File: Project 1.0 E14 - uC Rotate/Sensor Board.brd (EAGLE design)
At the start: 38.5 x 75 mm, 106 parts, among them IC1 LT1963EST-1.5, IC2 LT1963EST-1.5, IC4 LT1963EST-1.5, J1 501568-0207, J2 501568-0207, J3 SD-105027-101, J4 501568-0407, U1 MAG3110, U10 ADXL362, U11 TM4C1233H6PM, U14 TXB0108, U15 ADT7301, U17 LSM9DS0, U19 MAX21000, U2 H3LIS331DLTR, U21 SN74HC42, U22 SI7013, U3 L3GD20H, U4 LPS331AP, U5 MPL3115A2, U6 LSM303D, U8 STLM20, U9 LIS3DH, X1 32.768 kHz, X2 16.000 MHz

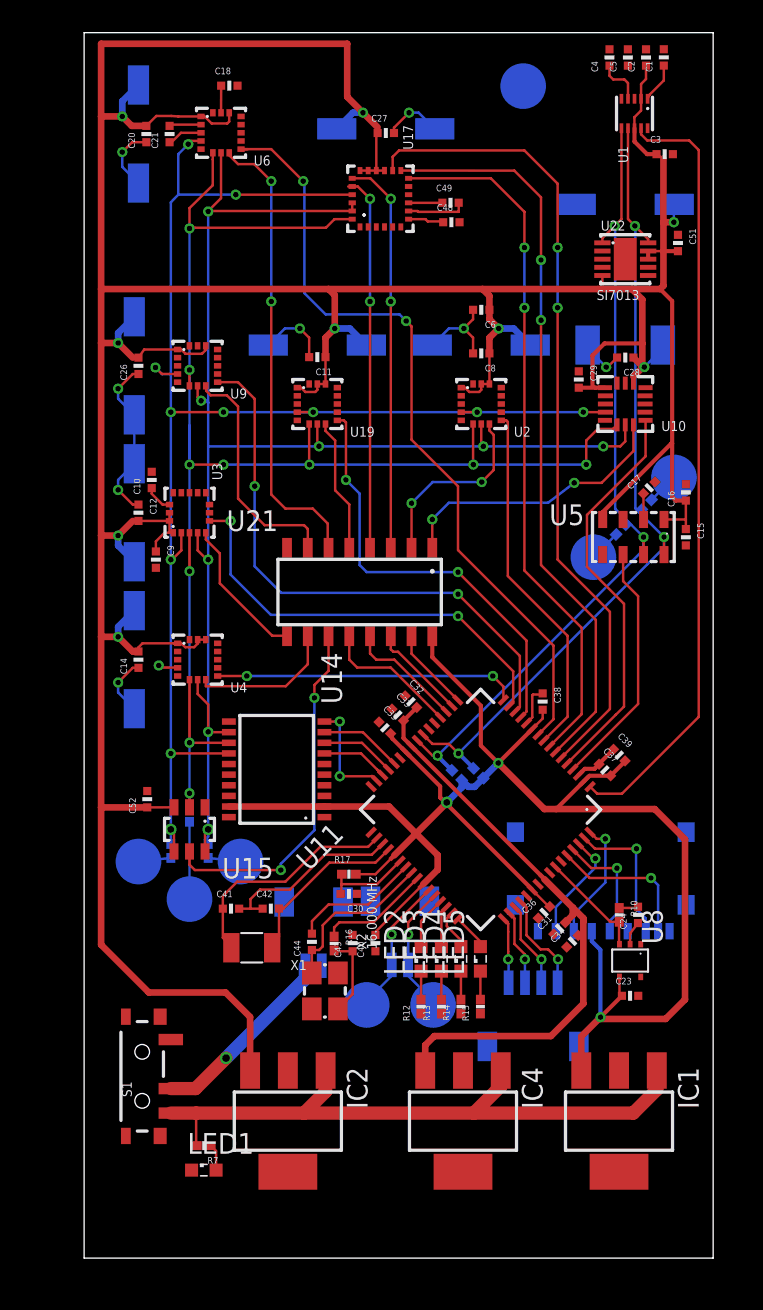
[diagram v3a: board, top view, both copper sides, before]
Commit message: Sensor Test Board: Completed power routing, Removed 1.2V regulator as this is not needed per the Tiva c datasheet. Power regulators and their respective circuits have been added for both 3.3-A and 3.3-B power rails. Swich has been moved to the bottom layer and is now positined facing the bottom of the board.
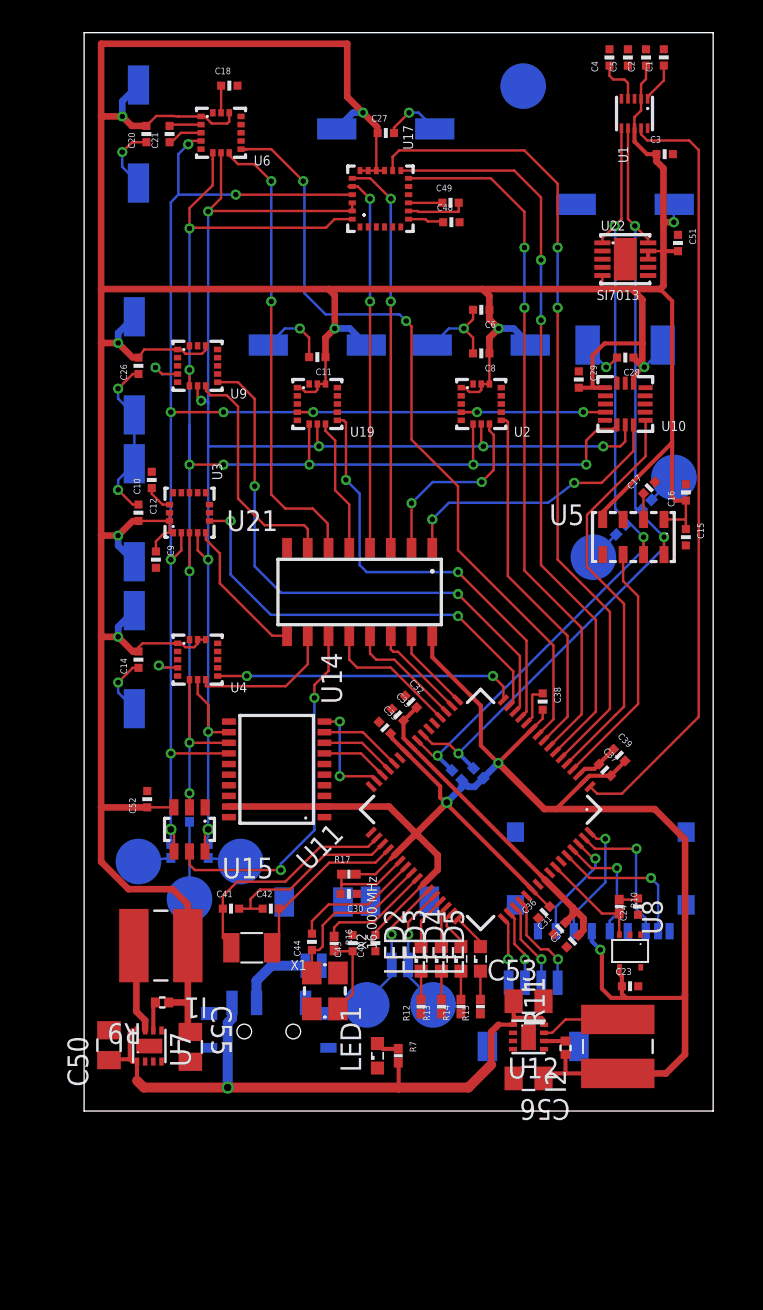
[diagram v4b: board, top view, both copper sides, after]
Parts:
- removed IC1, IC2, IC4: LT1963EST-1.5, linear-technology:SOT223
- added C50, C53: GRM21BR60J106ME19L, Power Regulator:0805
- added C55, C56: C2012X5R0J226M, Power Regulator:0805
- added I1, I2: SDR0403-1R0ML, Power Regulator:SDR0403
- added R11, R9: CRCW0402178KFKED, Power Regulator:0402
- added U12, U7: TPS62082DSGR, Power Regulator:S-PWSON-N8
- moved R7 13.1 mm to (20.7, 12.4), turned to 270 degrees
- moved LED1 12.7 mm to (19.5, 12.4), turned to 90 degrees
- moved S1 8.22 mm to (12.8, 13.9), flipped to the bottom, turned to 180 degrees
- moved C23 0.58 mm to (34.9, 16.6)
- moved U8 0.58 mm to (34.9, 18.8)
- moved C24 0.51 mm to (35.4, 21.5)
- moved R10 0.51 mm to (34.3, 21.5)
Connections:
- new net N$13: I1.2, U7.7
- new net N$23: R9.2, U7.6
- new net N$36: I2.2, U12.7
- new net N$37: R11.2, U12.6
- net 1.2V: no longer IC4.3
- net 3.3V-A: now also C55.1, I1.1, R9.1; no longer IC2.3
- net 3.3V-B: now also C56.1, I2.1, R11.1; no longer IC1.3
- net GND: now also C50.2, C53.2, C55.2, C56.2, U12.2, U12.3, U12.9, U7.2, U7.3, U7.9; no longer IC1.2, IC1.4, IC2.2, IC2.4, IC4.2, IC4.4
- net POWER-IN: now also C50.1, C53.1, U12.1, U12.8, U7.1, U7.8; no longer IC1.1, IC2.1, IC4.1
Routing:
- net 1.2V: track 37.5 -> 20.2 mm
- net N$2: track 11.8 -> 4.73 mm, vias 1 -> 0
- net 3.3V-B: track 110.9 -> 117.7 mm
- net N$13: track 0.00 -> 5.48 mm
- net N$36: track 0.00 -> 4.85 mm
- net 3.3V-A: track 257.4 -> 253.4 mm
- net POWER-IN: track 40.0 -> 41.9 mm, vias 0 -> 1
- net N$23: track 0.00 -> 1.77 mm
- net GND: track 60.6 -> 59.2 mm
- net N$37: track 0.00 -> 1.31 mm
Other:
- board size 38.5 x 75 mm -> 38.5 x 66 mm

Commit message: Sensor Test Board: Corrected LED footprint, Rerouted power under the uC to remove power traces from directly under uC. Moved sensor power rail further from edge of PCB to allow for GND plain to fully surround power rail.
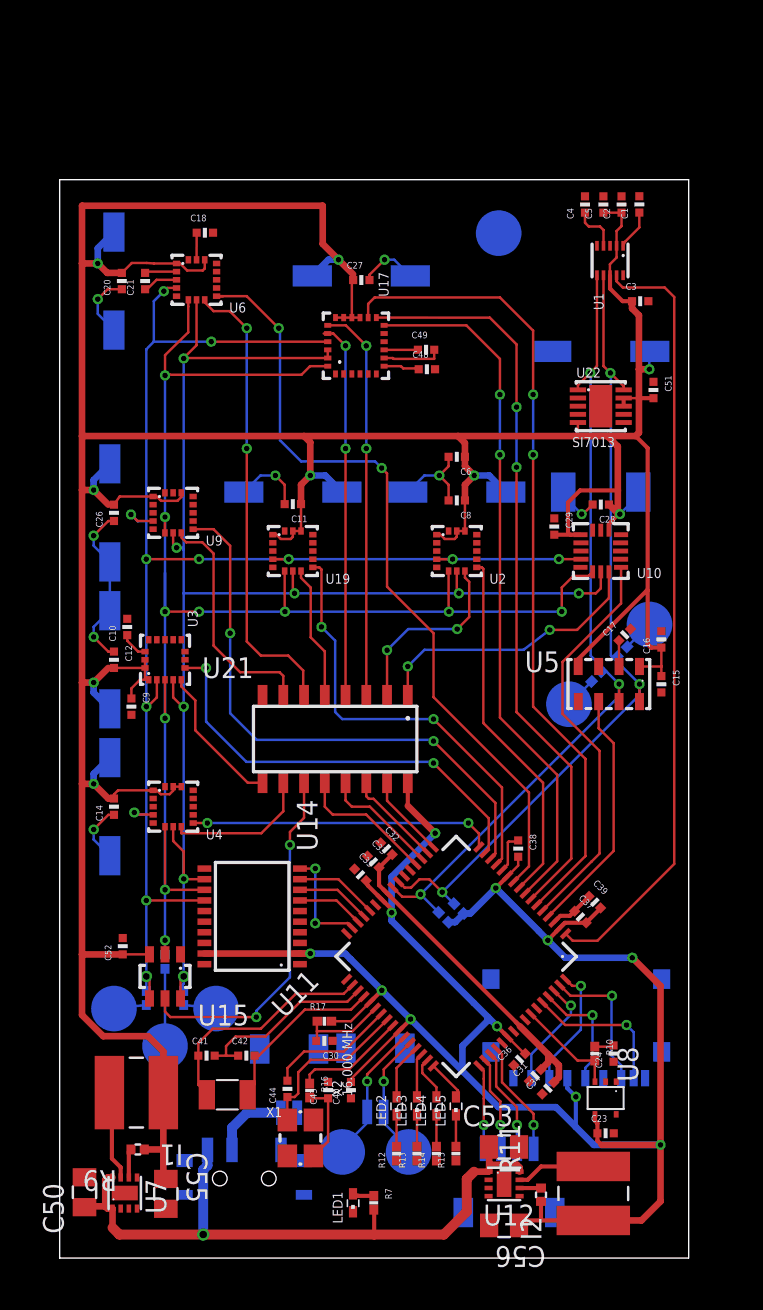
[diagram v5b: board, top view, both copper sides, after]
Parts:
- LED1: device eagle-ltspice:LED_SML0603 -> Kas-Diodes-LEDs:LED_0402
- LED2, LED3, LED4, LED5: value Green -> Red; device eagle-ltspice:LED_SML0603 -> Kas-Diodes-LEDs:LED_0402
- moved J4 10.3 mm to (27.5, 2.79)
- moved C10 9.12 mm to (4.14, 38.6)
- moved C11 9.12 mm to (14.3, 46.1)
- moved C12 9.12 mm to (3.33, 36.6)
- moved C13 9.12 mm to (3.07, 36.6)
- moved C14 9.12 mm to (3.33, 27.6)
- moved C16 9.12 mm to (36.8, 37.9)
- moved C17 9.12 mm to (34.6, 38.1)
- moved C19 9.12 mm to (33.1, 46.9)
- moved C2 9.12 mm to (34.4, 64.5)
- moved C20 9.12 mm to (3.81, 59.8)
- moved C21 9.12 mm to (5.23, 59.8)
- moved C22 9.12 mm to (33.1, 55.5)
- moved C28 9.12 mm to (33.1, 46.1)
- moved C32 9.12 mm to (20.0, 25.1)
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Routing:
- net 3.3V-B: track 117.7 -> 126.8 mm, vias 3 -> 11
- net 3.3V-A: track 253.4 -> 250.3 mm
- net SWO: track 4.04 -> 5.22 mm
- net TDI: track 4.66 -> 5.84 mm
- net SWDIO: track 5.32 -> 6.46 mm
- net SWCLK: track 6.19 -> 7.08 mm
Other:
- board text removed: "Dimensions goal = 38.5x67mm $19.991200372"
